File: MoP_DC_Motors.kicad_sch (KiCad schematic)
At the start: 20 parts, among them J501 Encoder1, J502 Encoder2, J503 1x2_Terminal, J504 1x2_Terminal, U4 L293D, U501 74LVC2G14

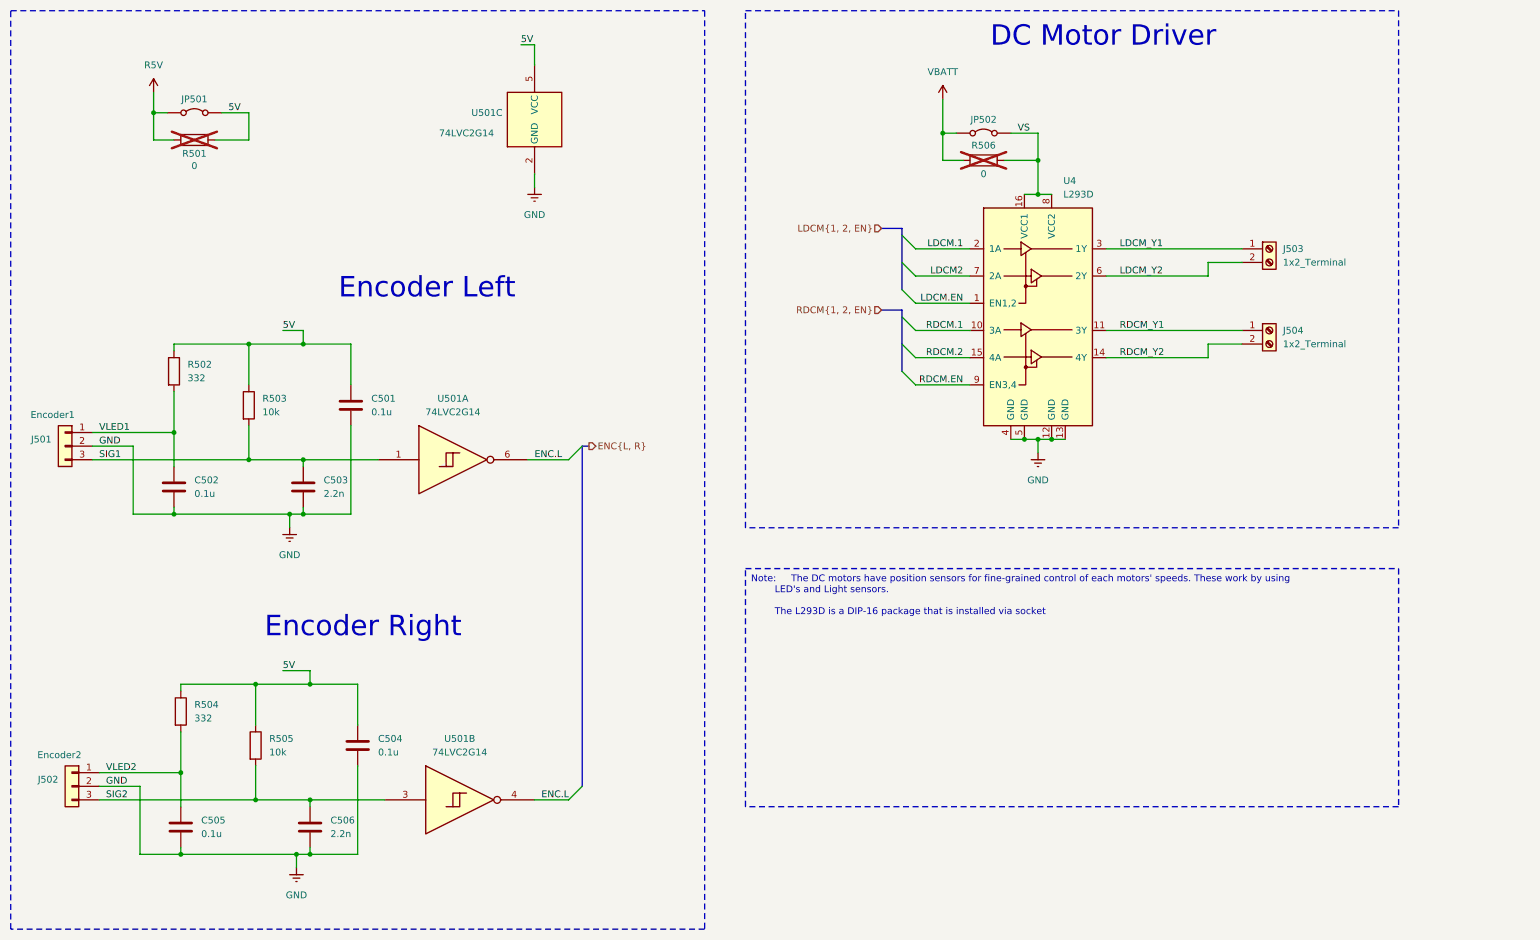
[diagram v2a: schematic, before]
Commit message: Added subproject for EPS PCB
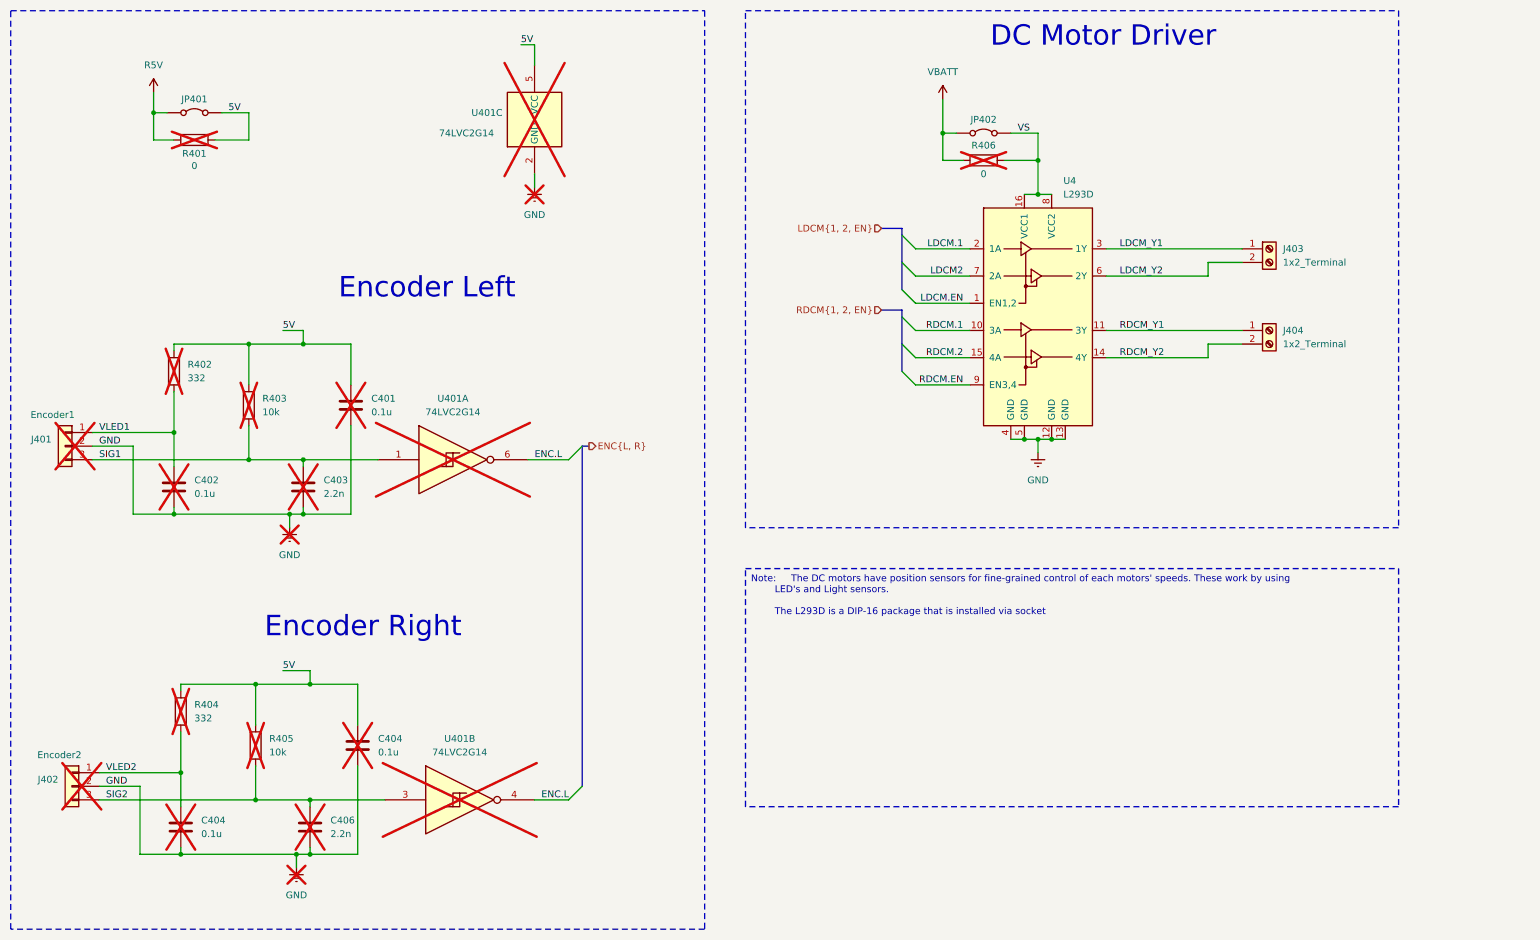
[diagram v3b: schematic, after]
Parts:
- C401: renamed from C501; now not fitted
- C402: renamed from C502; now not fitted
- C403: renamed from C503; now not fitted
- C404: renamed from C505; now not fitted
- C404: renamed from C504; now not fitted
- C406: renamed from C506; now not fitted
- J401: renamed from J501; now not fitted
- J402: renamed from J502; now not fitted
- R402: renamed from R502; now not fitted
- R403: renamed from R503; now not fitted
- R404: renamed from R504; now not fitted
- R405: renamed from R505; now not fitted
- U401: renamed from U501; now not fitted
- renumbered J503 to J403, J504 to J404, JP501 to JP401, JP502 to JP402, R501 to R401, R506 to R406

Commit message: added OBC
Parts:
- C401, C402, C403, C404, C406, J401, J402, R402, R403, R404, R405, U401: now fitted
- J403, J404, JP402, U4: now not fitted
- R401: now left out of the parts list
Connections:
- net ENC.L: no longer U401.4
- net LDCM2 renamed LDCM.2
- new net ENC.R: U401.4
